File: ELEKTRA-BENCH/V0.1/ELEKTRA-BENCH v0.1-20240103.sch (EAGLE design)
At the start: 37 parts, among them U2 LMR14030, U3 MP1601GTF-Z

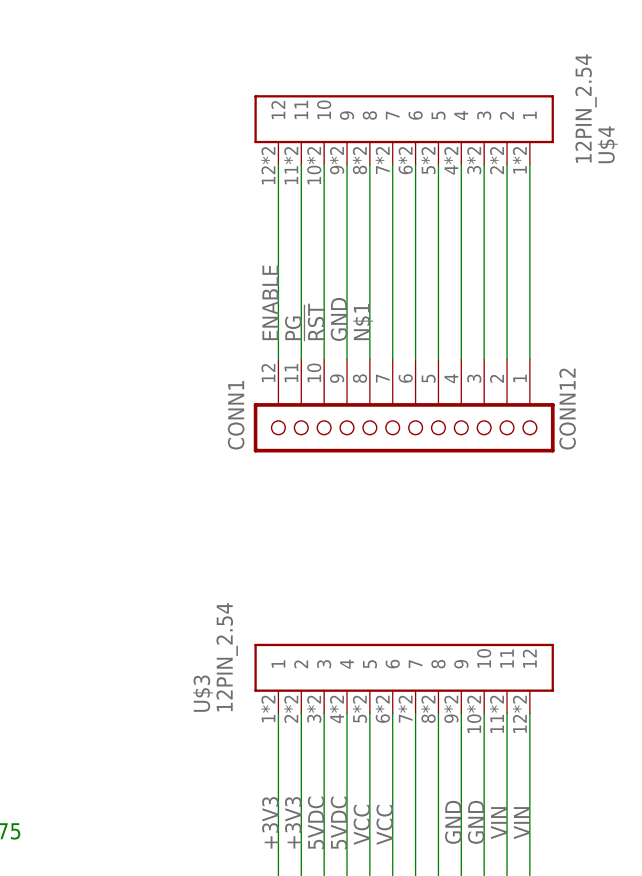
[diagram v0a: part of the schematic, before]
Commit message: Design elektra PMIC and Bench modules
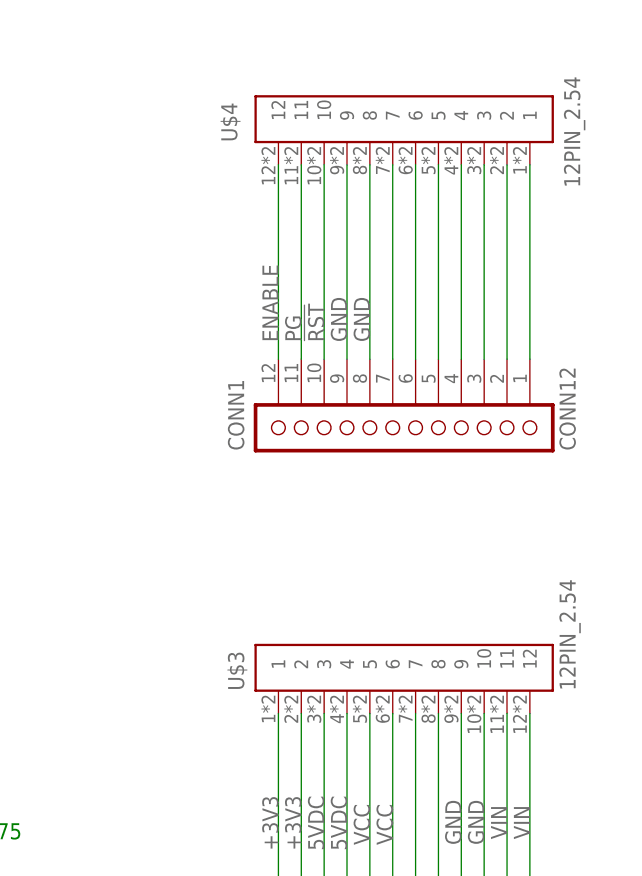
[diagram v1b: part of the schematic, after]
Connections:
- removed net N$1: CONN1.8, U$4.8
- net GND: now also CONN1.8, U$4.8
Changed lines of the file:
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@@
 </instance>
 <instance part="U$3" gate="G$1" x="270.51" y="62.23" smashed="yes" rot="R90">
-<attribute name="NAME" x="234.95" y="59.69" size="1.778" layer="95" rot="R90"/>
-<attribute name="VALUE" x="237.49" y="59.69" size="1.778" layer="96" rot="R90"/>
+<attribute name="NAME" x="238.76" y="62.23" size="1.778" layer="95" rot="R90"/>
+<attribute name="VALUE" x="275.59" y="62.23" size="1.778" layer="96" rot="R90"/>
 </instance>
 <instance part="U$4" gate="G$1" x="242.57" y="123.19" smashed="yes" rot="MR90">
-<attribute name="NAME" x="278.13" y="120.65" size="1.778" layer="95" rot="MR90"/>
-<attribute name="VALUE" x="275.59" y="120.65" size="1.778" layer="96" rot="MR90"/>
+<attribute name="NAME" x="236.22" y="123.19" size="1.778" layer="95" rot="MR90"/>
+<attribute name="VALUE" x="274.32" y="118.11" size="1.778" layer="96" rot="MR90"/>
 </instance>
 </instances>
@@
 <pinref part="U$3" gate="G$1" pin="10"/>
 <label x="265.43" y="45.085" size="1.778" layer="95" rot="R90"/>
+</segment>
+<segment>
+<pinref part="CONN1" gate="CONN1" pin="8"/>
+<wire x1="252.73" y1="99.06" x2="252.73" y2="120.65" width="0.1524" layer="91"/>
+<label x="252.73" y="100.965" size="1.778" layer="95" rot="R90"/>
+<pinref part="U$4" gate="G$1" pin="8"/>
 </segment>
 </net>
@@
 </segment>
 </net>
-<net name="N$1" class="0">
-<segment>
-<pinref part="CONN1" gate="CONN1" pin="8"/>
-<wire x1="252.73" y1="99.06" x2="252.73" y2="120.65" width="0.1524" layer="91"/>
-<label x="252.73" y="100.965" size="1.778" layer="95" rot="R90"/>
-<pinref part="U$4" gate="G$1" pin="8"/>
-</segment>
-</net>

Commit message: upload PCB and sch
upload PCB and sch
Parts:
- R2: value 39.2K -> 12K
- R3: value 30K -> 82K
- R4: value 47K -> 82K
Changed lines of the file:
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@@
 <part name="CONN2" library="particle-studios" library_urn="urn:adsk.eagle:library:10700396" deviceset="CONN12" device="" package3d_urn="urn:adsk.eagle:package:32962518/1"/>
 <part name="C4" library="particle SZ" library_urn="urn:adsk.eagle:library:21650216" deviceset="CAP" device="0402A" package3d_urn="urn:adsk.eagle:package:21650778/5" value="0.027uF"/>
-<part name="R2" library="particle SZ" library_urn="urn:adsk.eagle:library:21650216" deviceset="RES" device="0402S" package3d_urn="urn:adsk.eagle:package:21650840/5" value="39.2K"/>
+<part name="R2" library="particle SZ" library_urn="urn:adsk.eagle:library:21650216" deviceset="RES" device="0402S" package3d_urn="urn:adsk.eagle:package:21650840/5" value="12K"/>
 <part name="C1" library="particle SZ" library_urn="urn:adsk.eagle:library:21650216" deviceset="CAP" device="0402A" package3d_urn="urn:adsk.eagle:package:21650778/5" value="0.1uF"/>
 <part name="C8" library="particle SZ" library_urn="urn:adsk.eagle:library:21650216" deviceset="CAP" device="0402A" package3d_urn="urn:adsk.eagle:package:21650778/5" value="NC-33pF"/>
-<part name="R3" library="particle SZ" library_urn="urn:adsk.eagle:library:21650216" deviceset="RES" device="0402S" package3d_urn="urn:adsk.eagle:package:21650840/5" value="30K"/>
-<part name="R4" library="particle SZ" library_urn="urn:adsk.eagle:library:21650216" deviceset="RES" device="0402S" package3d_urn="urn:adsk.eagle:package:21650840/5" value="47K"/>
+<part name="R3" library="particle SZ" library_urn="urn:adsk.eagle:library:21650216" deviceset="RES" device="0402S" package3d_urn="urn:adsk.eagle:package:21650840/5" value="82K"/>
+<part name="R4" library="particle SZ" library_urn="urn:adsk.eagle:library:21650216" deviceset="RES" device="0402S" package3d_urn="urn:adsk.eagle:package:21650840/5" value="82K"/>
 <part name="R5" library="particle SZ" library_urn="urn:adsk.eagle:library:21650216" deviceset="RES" device="0402S" package3d_urn="urn:adsk.eagle:package:21650840/5" value="39.2K"/>
 <part name="C9" library="Particle" deviceset="CAP_1" device="" value="0.1uF"/>
